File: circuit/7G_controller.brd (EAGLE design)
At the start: 63 x 70.5 mm, 22 parts, among them Q1 32768Hz, T1 TPS1101D

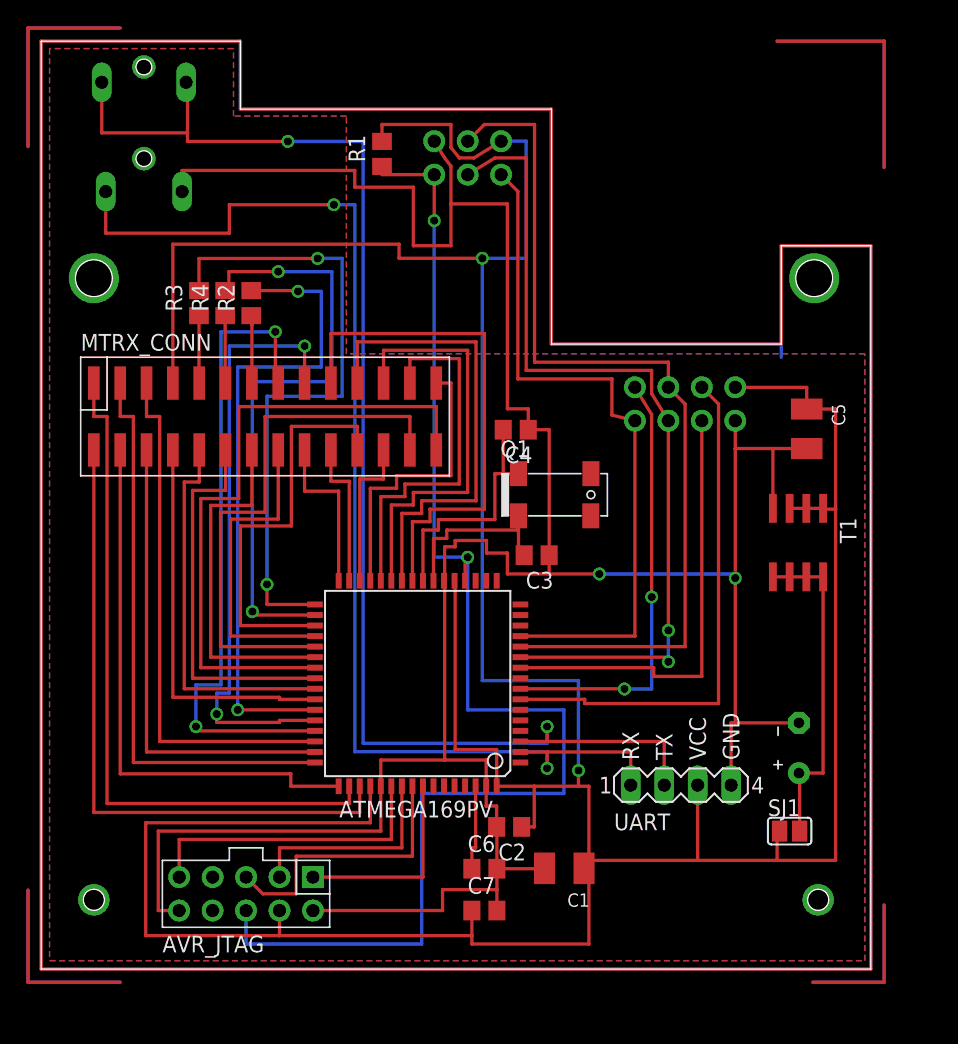
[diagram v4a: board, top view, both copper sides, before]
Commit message: 
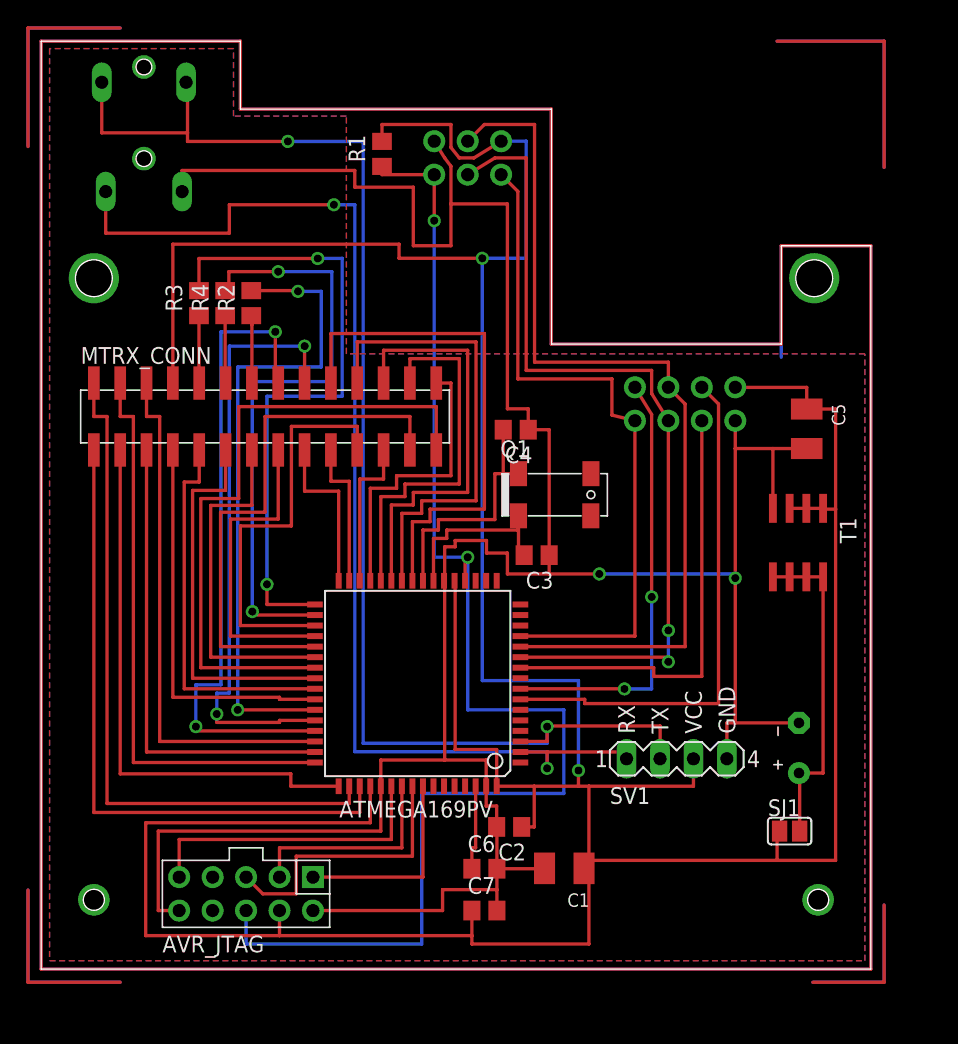
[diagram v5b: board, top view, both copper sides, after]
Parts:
- removed UART: (no value), KileParts:UART_PORT
- added SV1: (no value), KileParts:UART_PORT
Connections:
- net GND: now also SV1.GND; no longer UART.GND
- net N$29: now also SV1.RX; no longer UART.RX
- net N$30: now also SV1.TX; no longer UART.TX
- net VCC: now also SV1.VCC; no longer UART.+5V
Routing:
- net VCC: track 292.7 -> 297.0 mm
- net N$29: track 93.8 -> 91.5 mm
- net GND: track 225.4 -> 223.7 mm
- net N$30: track 104.5 -> 103.4 mm
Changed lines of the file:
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@@
 <setting verticaltext="up"/>
 </settings>
-<grid distance="0.05" unitdist="inch" unit="mm" style="lines" multiple="1" display="yes" altdistance="0.025" altunitdist="inch" altunit="inch"/>
+<grid distance="0.00625" unitdist="inch" unit="inch" style="lines" multiple="1" display="yes" altdistance="0.025" altunitdist="inch" altunit="inch"/>
 <layers>
 <layer number="1" name="Top" color="4" fill="1" visible="yes" active="yes"/>
@@
 <element name="MTRX_CONN" library="KileParts" package="SS7G_CONN_SMD" value="SS7G_CONNSMD" x="17" y="44.5"/>
 <element name="BAT1" library="KileParts" package="BATTERY" value="" x="57.54" y="19.33" rot="R90"/>
-<element name="UART" library="KileParts" package="UART_PORT" value="" x="48.5775" y="16.51">
-<attribute name="OC_NEWARK" value="unknown" x="48.5775" y="16.51" size="1.778" layer="27" display="off"/>
-<attribute name="MPN" value="" x="48.5775" y="16.51" size="1.778" layer="27" display="off"/>
-<attribute name="MF" value="" x="48.5775" y="16.51" size="1.778" layer="27" display="off"/>
-<attribute name="OC_FARNELL" value="unknown" x="48.5775" y="16.51" size="1.778" layer="27" display="off"/>
-</element>
 <element name="C5" library="rcl" package="SMC_B" value="4.7uF" x="58.13125" y="43.5675" rot="R270"/>
 <element name="R2" library="rcl" package="R0805" value="470R" x="15.9512" y="53.11" rot="R90"/>
@@
 <element name="C7" library="rcl" package="C0805" value="100nF" x="33.655" y="6.985"/>
 <element name="DBG_JACK" library="KileParts" package="JACK_CHEAP" value="JACK_FEMALE_3.5MMCHEAP" x="7.8" y="69.58" rot="MR0"/>
+<element name="SV1" library="KileParts" package="UART_PORT" value="" x="48.26" y="18.51">
+<attribute name="OC_NEWARK" value="unknown" x="48.26" y="18.51" size="1.778" layer="27" display="off"/>
+<attribute name="MPN" value="" x="48.26" y="18.51" size="1.778" layer="27" display="off"/>
+<attribute name="MF" value="" x="48.26" y="18.51" size="1.778" layer="27" display="off"/>
+<attribute name="OC_FARNELL" value="unknown" x="48.26" y="18.51" size="1.778" layer="27" display="off"/>
+</element>
 </elements>
 <signals>
@@
 <contactref element="AVR_ISP" pad="VCC"/>
 <contactref element="MTRX_CONN" pad="4"/>
-<contactref element="UART" pad="+5V"/>
 <contactref element="AVR_JTAG" pad="P$4"/>
 <wire x1="32.86125" y1="64.135" x2="31.75" y2="64.135" width="0.254" layer="1"/>
@@
 <wire x1="10" y1="47.04" x2="10" y2="57.58375" width="0.254" layer="1"/>
 <wire x1="37.43875" y1="16.425" x2="34.59" y2="16.425" width="0.254" layer="1"/>
-<wire x1="49.8475" y1="10.795" x2="49.8475" y2="16.51" width="0.254" layer="1"/>
 <wire x1="31.39" y1="32.025" x2="31.4325" y2="32.025" width="0.254" layer="1"/>
 <wire x1="31.4325" y1="32.025" x2="31.4325" y2="19.20875" width="0.254" layer="1"/>
@@
 <wire x1="60.325" y1="37.465" x2="60.325" y2="10.795" width="0.254" layer="1"/>
 <wire x1="60.325" y1="10.795" x2="55.88" y2="10.795" width="0.254" layer="1"/>
-<wire x1="55.88" y1="10.795" x2="49.8475" y2="10.795" width="0.254" layer="1"/>
-<wire x1="49.8475" y1="10.795" x2="41.5925" y2="10.795" width="0.254" layer="1"/>
+<wire x1="55.88" y1="10.795" x2="41.5925" y2="10.795" width="0.254" layer="1"/>
+<contactref element="SV1" pad="VCC"/>
+<wire x1="41.5925" y1="16.425" x2="49.53" y2="16.425" width="0.254" layer="1"/>
+<wire x1="49.53" y1="16.425" x2="49.53" y2="18.51" width="0.254" layer="1"/>
 </signal>
 <signal name="GND">
@@
 <contactref element="C4" pad="1"/>
 <contactref element="BAT1" pad="-"/>
-<contactref element="UART" pad="GND"/>
 <contactref element="AVR_ISP" pad="GND"/>
 <contactref element="AVR_JTAG" pad="P$10"/>
@@
 <wire x1="30.63875" y1="18.415" x2="25.79" y2="18.415" width="0.254" layer="1"/>
 <wire x1="25.79" y1="18.415" x2="25.79" y2="16.425" width="0.254" layer="1"/>
-<wire x1="52.3875" y1="16.51" x2="52.3875" y2="21.235" width="0.254" layer="1"/>
 <wire x1="57.54" y1="21.235" x2="52.705" y2="21.235" width="0.254" layer="1"/>
-<wire x1="52.705" y1="21.235" x2="52.3875" y2="21.235" width="0.254" layer="1"/>
 <wire x1="30.59" y1="32.025" x2="30.63875" y2="32.025" width="0.254" layer="1"/>
 <wire x1="30.63875" y1="32.025" x2="30.63875" y2="18.415" width="0.254" layer="1"/>
@@
 <wire x1="10.7" y1="61.58" x2="10.7" y2="63.1825" width="0.254" layer="1"/>
 <wire x1="10.7" y1="63.1825" x2="23.8125" y2="63.1825" width="0.254" layer="1"/>
+<contactref element="SV1" pad="GND"/>
+<wire x1="52.705" y1="21.235" x2="52.07" y2="21.235" width="0.254" layer="1"/>
+<wire x1="52.07" y1="21.235" x2="52.07" y2="18.51" width="0.254" layer="1"/>
 </signal>
 <signal name="MOSI">
@@
 <signal name="N$29">
 <contactref element="ATMEGA169PV" pad="2"/>
-<contactref element="UART" pad="RX"/>
 <wire x1="36.39" y1="19.025" x2="38.4175" y2="19.025" width="0.254" layer="1"/>
-<wire x1="38.4175" y1="19.025" x2="44.7675" y2="19.025" width="0.254" layer="1"/>
-<wire x1="44.7675" y1="19.025" x2="44.7675" y2="16.51" width="0.254" layer="1"/>
 <contactref element="DBG_JACK" pad="4"/>
 <wire x1="22.225" y1="60.58" x2="23.8125" y2="60.58" width="0.254" layer="16"/>
@@
 <wire x1="14.2875" y1="58.42" x2="4.9" y2="58.42" width="0.254" layer="1"/>
 <wire x1="4.9" y1="58.42" x2="4.9" y2="61.58" width="0.254" layer="1"/>
+<contactref element="SV1" pad="RX"/>
+<wire x1="38.4175" y1="19.025" x2="44.45" y2="19.025" width="0.254" layer="1"/>
+<wire x1="44.45" y1="19.025" x2="44.45" y2="18.51" width="0.254" layer="1"/>
 </signal>
 <signal name="N$30">
 <contactref element="ATMEGA169PV" pad="3"/>
-<contactref element="UART" pad="TX"/>
 <wire x1="36.39" y1="19.825" x2="38.4175" y2="19.825" width="0.254" layer="1"/>
-<wire x1="38.4175" y1="19.825" x2="47.3075" y2="19.825" width="0.254" layer="1"/>
-<wire x1="47.3075" y1="19.825" x2="47.3075" y2="16.51" width="0.254" layer="1"/>
 <contactref element="DBG_JACK" pad="2"/>
 <contactref element="DBG_JACK" pad="3"/>
@@
 <wire x1="11.1125" y1="66.04" x2="11.1125" y2="68.88" width="0.254" layer="1"/>
 <wire x1="11.1125" y1="68.88" x2="11" y2="69.88" width="0.254" layer="1"/>
+<contactref element="SV1" pad="TX"/>
+<wire x1="46.99" y1="18.51" x2="47" y2="18.51" width="0.254" layer="1"/>
+<wire x1="47" y1="18.51" x2="47" y2="21" width="0.254" layer="1"/>
+<wire x1="47" y1="21" x2="38.4175" y2="21" width="0.254" layer="1"/>
+<wire x1="38.4175" y1="21" x2="38.4175" y2="20.955" width="0.254" layer="1"/>
 </signal>
 <signal name="IRQ">

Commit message: 
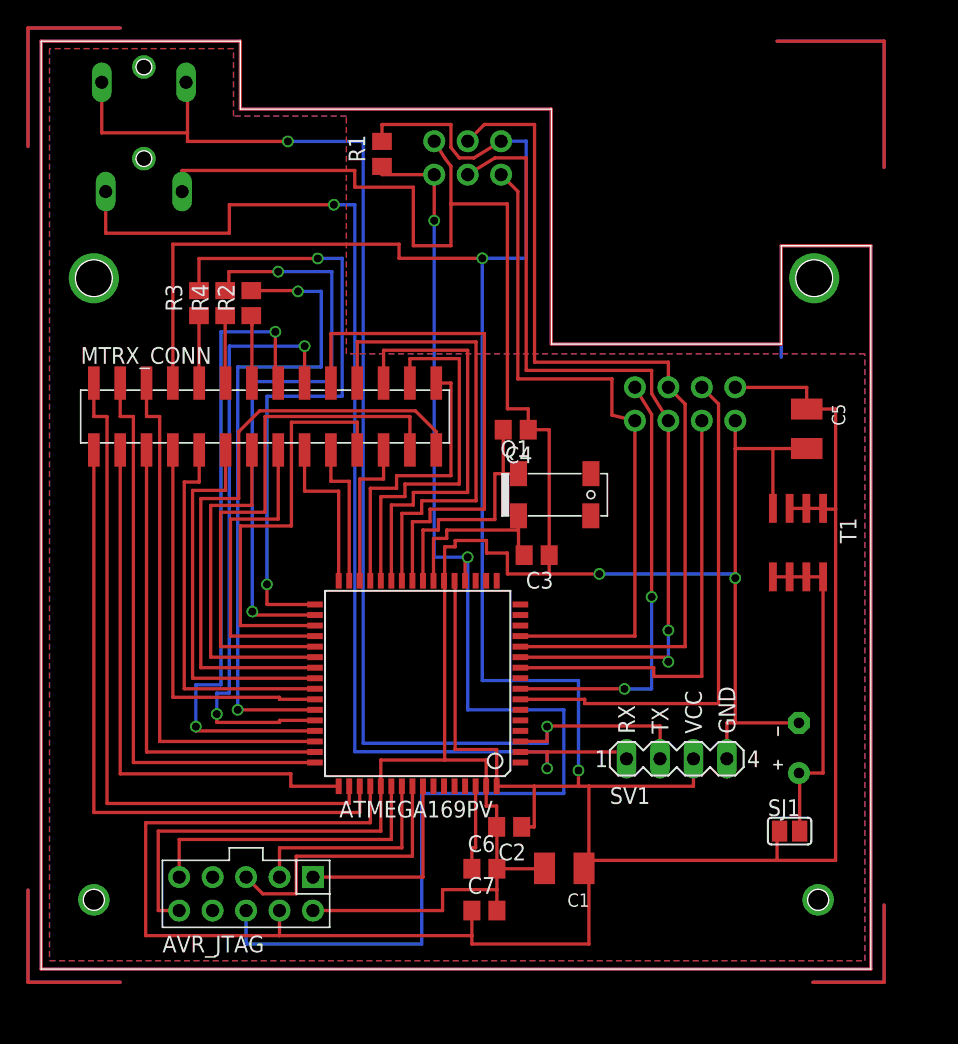
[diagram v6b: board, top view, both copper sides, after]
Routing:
- net H28: track 49.7 -> 47.2 mm
- net H25: track 31.5 -> 32.1 mm
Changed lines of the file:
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@@
 <setting verticaltext="up"/>
 </settings>
-<grid distance="0.00625" unitdist="inch" unit="inch" style="lines" multiple="1" display="yes" altdistance="0.025" altunitdist="inch" altunit="inch"/>
+<grid distance="0.1" unitdist="mm" unit="mm" style="lines" multiple="1" display="yes" altdistance="0.025" altunitdist="inch" altunit="inch"/>
 <layers>
 <layer number="1" name="Top" color="4" fill="1" visible="yes" active="yes"/>
@@
 <layer number="54" name="bGND_GNDA" color="1" fill="9" visible="no" active="no"/>
 <layer number="56" name="wert" color="7" fill="1" visible="no" active="no"/>
+<layer number="57" name="tCAD" color="7" fill="1" visible="no" active="no"/>
 <layer number="91" name="Nets" color="2" fill="1" visible="no" active="no"/>
 <layer number="92" name="Busses" color="1" fill="1" visible="no" active="no"/>
@@
 <layer number="132" name="bAdjust" color="7" fill="1" visible="no" active="yes"/>
 <layer number="144" name="Drill_legend" color="7" fill="1" visible="no" active="yes"/>
+<layer number="150" name="Notes" color="7" fill="1" visible="no" active="yes"/>
 <layer number="151" name="HeatSink" color="7" fill="1" visible="no" active="yes"/>
 <layer number="152" name="_bDocu" color="7" fill="1" visible="no" active="yes"/>
+<layer number="153" name="FabDoc1" color="6" fill="1" visible="no" active="no"/>
+<layer number="154" name="FabDoc2" color="2" fill="1" visible="no" active="no"/>
+<layer number="155" name="FabDoc3" color="7" fill="15" visible="no" active="no"/>
 <layer number="199" name="Contour" color="7" fill="1" visible="no" active="yes"/>
 <layer number="200" name="200bmp" color="1" fill="10" visible="no" active="no"/>
@@
 </class>
 </classes>
-<designrules name="default *">
+<designrules name="ITEADstudio_DRC">
 <description language="de">&lt;b&gt;EAGLE Design Rules&lt;/b&gt;
 &lt;p&gt;
@@
 necessary adjustments and save your customized
 design rules under a new name.</description>
+<description language="zh">&lt;b&gt;Seeed Studio EAGLE Design Rules&lt;/b&gt;
+</description>
 <param name="layerSetup" value="(1*16)"/>
 <param name="mtCopper" value="0.035mm 0.035mm 0.035mm 0.035mm 0.035mm 0.035mm 0.035mm 0.035mm 0.035mm 0.035mm 0.035mm 0.035mm 0.035mm 0.035mm 0.035mm 0.035mm"/>
 <param name="mtIsolate" value="1.5mm 0.15mm 0.2mm 0.15mm 0.2mm 0.15mm 0.2mm 0.15mm 0.2mm 0.15mm 0.2mm 0.15mm 0.2mm 0.15mm 0.2mm"/>
-<param name="mdWireWire" value="10mil"/>
-<param name="mdWirePad" value="10mil"/>
-<param name="mdWireVia" value="10mil"/>
-<param name="mdPadPad" value="10mil"/>
-<param name="mdPadVia" value="10mil"/>
-<param name="mdViaVia" value="10mil"/>
-<param name="mdSmdPad" value="10mil"/>
-<param name="mdSmdVia" value="10mil"/>
-<param name="mdSmdSmd" value="10mil"/>
+<param name="mdWireWire" value="6mil"/>
+<param name="mdWirePad" value="6mil"/>
+<param name="mdWireVia" value="6mil"/>
+<param name="mdPadPad" value="6mil"/>
+<param name="mdPadVia" value="6mil"/>
+<param name="mdViaVia" value="6mil"/>
+<param name="mdSmdPad" value="0mil"/>
+<param name="mdSmdVia" value="0mil"/>
+<param name="mdSmdSmd" value="0mil"/>
 <param name="mdViaViaSameLayer" value="8mil"/>
 <param name="mnLayersViaInSmd" value="2"/>
-<param name="mdCopperDimension" value="40mil"/>
-<param name="mdDrill" value="8mil"/>
+<param name="mdCopperDimension" value="10mil"/>
+<param name="mdDrill" value="10mil"/>
 <param name="mdSmdStop" value="0mil"/>
-<param name="msWidth" value="10mil"/>
-<param name="msDrill" value="0.6mm"/>
-<param name="msMicroVia" value="9.99mm"/>
+<param name="msWidth" value="6mil"/>
+<param name="msDrill" value="12mil"/>
+<param name="msMicroVia" value="12mil"/>
 <param name="msBlindViaRatio" value="0.5"/>
 <param name="rvPadTop" value="0.25"/>
@@
 <param name="rlMinPadBottom" value="10mil"/>
 <param name="rlMaxPadBottom" value="20mil"/>
-<param name="rlMinViaOuter" value="8mil"/>
+<param name="rlMinViaOuter" value="6mil"/>
 <param name="rlMaxViaOuter" value="20mil"/>
-<param name="rlMinViaInner" value="8mil"/>
+<param name="rlMinViaInner" value="6mil"/>
 <param name="rlMaxViaInner" value="20mil"/>
 <param name="rlMinMicroViaOuter" value="4mil"/>
@@
 <param name="psTop" value="-1"/>
 <param name="psBottom" value="-1"/>
-<param name="psFirst" value="-1"/>
+<param name="psFirst" value="0"/>
 <param name="psElongationLong" value="100"/>
 <param name="psElongationOffset" value="100"/>
 <param name="mvStopFrame" value="1"/>
 <param name="mvCreamFrame" value="0"/>
-<param name="mlMinStopFrame" value="4mil"/>
-<param name="mlMaxStopFrame" value="4mil"/>
+<param name="mlMinStopFrame" value="2mil"/>
+<param name="mlMaxStopFrame" value="2mil"/>
 <param name="mlMinCreamFrame" value="0mil"/>
 <param name="mlMaxCreamFrame" value="0mil"/>
-<param name="mlViaStopLimit" value="0mil"/>
+<param name="mlViaStopLimit" value="100mil"/>
 <param name="srRoundness" value="0"/>
 <param name="srMinRoundness" value="0mil"/>
@@
 <param name="checkAngle" value="0"/>
 <param name="checkFont" value="1"/>
-<param name="checkRestrict" value="1"/>
+<param name="checkRestrict" value="0"/>
 <param name="useDiameter" value="13"/>
 <param name="maxErrors" value="50"/>
@@
 <contactref element="MTRX_CONN" pad="28"/>
 <contactref element="ATMEGA169PV" pad="39"/>
-<wire x1="30" y1="41.96" x2="30" y2="45.25" width="0.254" layer="1"/>
-<wire x1="30" y1="45.25" x2="15" y2="45.25" width="0.254" layer="1"/>
-<wire x1="15" y1="45.25" x2="15" y2="38.27" width="0.254" layer="1"/>
+<wire x1="28.4125" y1="44.9325" x2="16.5875" y2="44.9325" width="0.254" layer="1"/>
 <wire x1="15" y1="38.27" x2="12.1225" y2="38.27" width="0.254" layer="1"/>
 <wire x1="12.1225" y1="38.27" x2="12.1225" y2="25.425" width="0.254" layer="1"/>
 <wire x1="12.1225" y1="25.425" x2="20.79" y2="25.425" width="0.254" layer="1"/>
+<wire x1="30" y1="41.96" x2="30" y2="43.345" width="0.254" layer="1"/>
+<wire x1="30" y1="43.345" x2="28.4125" y2="44.9325" width="0.254" layer="1"/>
+<wire x1="15" y1="38.27" x2="15" y2="43.345" width="0.254" layer="1"/>
+<wire x1="15" y1="43.345" x2="16.5875" y2="44.9325" width="0.254" layer="1"/>
 </signal>
 <signal name="H27">
 <contactref element="MTRX_CONN" pad="27"/>
 <contactref element="ATMEGA169PV" pad="37"/>
-<wire x1="28" y1="41.96" x2="28" y2="44.5" width="0.254" layer="1"/>
 <wire x1="28" y1="44.5" x2="17" y2="44.5" width="0.254" layer="1"/>
 <wire x1="17" y1="44.5" x2="17" y2="37.23" width="0.254" layer="1"/>
@@
 <wire x1="13.6225" y1="37.23" x2="13.6225" y2="27.025" width="0.254" layer="1"/>
 <wire x1="13.6225" y1="27.025" x2="20.79" y2="27.025" width="0.254" layer="1"/>
+<wire x1="28" y1="44.5" x2="28" y2="41.96" width="0.254" layer="1"/>
 </signal>
 <signal name="H25">
 <contactref element="MTRX_CONN" pad="25"/>
 <contactref element="ATMEGA169PV" pad="35"/>
-<wire x1="24" y1="41.96" x2="24" y2="43.75" width="0.254" layer="1"/>
-<wire x1="24" y1="43.75" x2="19" y2="43.75" width="0.254" layer="1"/>
-<wire x1="19" y1="43.75" x2="19" y2="36.19" width="0.254" layer="1"/>
+<wire x1="24" y1="41.96" x2="24" y2="44.0675" width="0.254" layer="1"/>
+<wire x1="24" y1="44.0675" x2="19" y2="44.0675" width="0.254" layer="1"/>
+<wire x1="19" y1="44.0675" x2="19" y2="36.19" width="0.254" layer="1"/>
 <wire x1="19" y1="36.19" x2="15.1225" y2="36.19" width="0.254" layer="1"/>
 <wire x1="15.1225" y1="36.19" x2="15.1225" y2="28.625" width="0.254" layer="1"/>
